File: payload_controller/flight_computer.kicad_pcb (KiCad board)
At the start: 4 copper layers, 87 x 75 mm, 145 parts, among them J1 Silicon Cell, J2 G125-MH12605M4R, J3 Conn_01x08_Female, J4 Conn_02x07_Odd_Even, J5 0781710004, J6 Conn_01x03_Male, Q1 DMC2053UVT, U1 74HC590, U10 OPA2387, U11 MCP4725xxx-xCH, U12 ADS131M04IPWR, U13 INA190A4IDDFR, U15 SN74LVC1G14DRL, U16 CD4518BM96, U17 CD4028BMT, U18 CD4028BMT, U19 MAX4736EUBT, U2 ADG841YKSZ-500RL7, U20 MAX4736EUBT, U21 MAX4736EUBT, U22 MAX4736EUBT, U23 MAX4736EUBT, U24 MAX4736EUBT, U25 MAX4736EUBT, U26 MAX4736EUBT, U27 MAX4736EUBT, U28 MAX4736EUBT, U29 MAX4736EUBT, U3 ADG841YKSZ-500RL7, U30 LT3092EDD#TRPBF, U31 LT6654AMPS6-1.25, U33 ICL7660CSAT, U34 MSP430FR5969IRGZR, U4 ADG841YKSZ-500RL7, U5 ADG841YKSZ-500RL7, U6 ADG841YKSZ-500RL7, U7 ADG841YKSZ-500RL7, U8 ADG841YKSZ-500RL7, U9 ADG841YKSZ-500RL7, Y1 CM8V-T1A

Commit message: Continuing layout
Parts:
- moved R28 17.0 mm to (178.9, 129.4), turned to 270 degrees
- moved R29 13.7 mm to (180.5, 129.4), turned to 270 degrees
- moved C11 8.41 mm to (156.0, 113.8), turned to 0 degrees
- moved R30 7.15 mm to (183.8, 132.0)
- moved Q1 7.08 mm to (183.9, 129.4), turned to 0 degrees
- moved R12 6.65 mm to (140.3, 115.1), turned to 270 degrees
- moved C10 5.72 mm to (146.6, 96.1)
- moved U1 5.71 mm to (152.7, 96.1)
- moved U10 4.72 mm to (156.0, 116.0), turned to 0 degrees
- moved J4 4.57 mm to (119.4, 97.0)
- moved C41 3.80 mm to (186.9, 131.2)
- moved C37 3.05 mm to (158.8, 69.3)
- moved C38 3.05 mm to (144.5, 74.2)
- moved C39 3.05 mm to (158.8, 77.2)
- moved C40 3.05 mm to (146.5, 85.2)
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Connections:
- net /Payload Controller/BUSY_IN renamed Net-(U34-Pad19)
- J2 pad 10: /Perovskite Switches/ALERT -> /Payload Controller/ALERT
- J2 pad 25: /Perovskite Switches/ALERT -> /Payload Controller/ALERT
- J2 pad 7: /Perovskite Switches/ALERT -> /Payload Controller/ALERT
- J3 pad 5: FAULT -> PAYLOAD_RST
- J3 pad 6: PAYLOAD_RST -> FAULT
- U10 pad 1: /Curve Tracer/LADDER_VOLTAGE -> Net-(R23-Pad2)
- U10 pad 2: /Curve Tracer/LADDER_VOLTAGE -> Net-(R23-Pad2)
- U10 pad 3: Net-(R11-Pad2) -> Net-(R25-Pad1)
- U10 pad 5: Net-(R25-Pad1) -> /Curve Tracer/LADDER_VOLTAGE
- U10 pad 6: Net-(R23-Pad2) -> Net-(R11-Pad2)
- U10 pad 7: Net-(R23-Pad2) -> /Curve Tracer/LADDER_VOLTAGE
- U19 pad 10: Net-(J2-Pad1) -> Net-(U19-Pad10)
- U19 pad 2: GND -> /Perovskite Switches/PANEL_POSITIVE
- U19 pad 4: /Perovskite Switches/PANEL_POSITIVE -> GND
- U19 pad 6: Net-(U19-Pad6) -> Net-(J2-Pad1)
- U19 pad 7: GND -> /Perovskite Switches/PANEL_POSITIVE
- U19 pad 9: /Perovskite Switches/PANEL_POSITIVE -> GND
- U20 pad 1: Net-(U17-Pad14) -> Net-(U17-Pad9)
- U20 pad 2: Net-(U19-Pad6) -> Net-(U19-Pad10)
- U20 pad 4: Net-(U19-Pad6) -> Net-(U19-Pad10)
- U20 pad 5: Net-(U17-Pad15) -> Net-(U17-Pad7)
- U21 pad 1: Net-(U17-Pad2) -> Net-(U17-Pad6)
- U21 pad 2: Net-(U19-Pad6) -> Net-(U19-Pad10)
- U21 pad 4: Net-(U19-Pad6) -> Net-(U19-Pad10)
- U21 pad 5: Net-(U17-Pad1) -> Net-(U17-Pad5)
- U22 pad 2: Net-(U19-Pad6) -> Net-(U19-Pad10)
- U22 pad 4: Net-(U19-Pad6) -> Net-(U19-Pad10)
- U23 pad 1: Net-(U17-Pad6) -> Net-(U17-Pad2)
- U23 pad 2: Net-(U19-Pad6) -> Net-(U19-Pad10)
- U23 pad 4: Net-(U19-Pad6) -> Net-(U19-Pad10)
- U23 pad 5: Net-(U17-Pad5) -> Net-(U17-Pad1)
- U24 pad 1: Net-(U17-Pad9) -> Net-(U17-Pad14)
- U24 pad 2: Net-(U19-Pad6) -> Net-(U19-Pad10)
- U24 pad 4: Net-(U19-Pad6) -> Net-(U19-Pad10)
- U24 pad 5: Net-(U17-Pad7) -> Net-(U17-Pad15)
- U25 pad 1: Net-(U18-Pad14) -> Net-(U18-Pad9)
- U25 pad 2: Net-(U19-Pad6) -> Net-(U19-Pad10)
- U25 pad 4: Net-(U19-Pad6) -> Net-(U19-Pad10)
- U25 pad 5: Net-(U18-Pad15) -> Net-(U18-Pad7)
- U26 pad 1: Net-(U18-Pad2) -> Net-(U18-Pad6)
- U26 pad 2: Net-(U19-Pad6) -> Net-(U19-Pad10)
- U26 pad 4: Net-(U19-Pad6) -> Net-(U19-Pad10)
- U26 pad 5: Net-(U18-Pad1) -> Net-(U18-Pad5)
- U27 pad 2: Net-(U19-Pad6) -> Net-(U19-Pad10)
- U27 pad 4: Net-(U19-Pad6) -> Net-(U19-Pad10)
- U28 pad 1: Net-(U18-Pad6) -> Net-(U18-Pad2)
- U28 pad 2: Net-(U19-Pad6) -> Net-(U19-Pad10)
- U28 pad 4: Net-(U19-Pad6) -> Net-(U19-Pad10)
- U28 pad 5: Net-(U18-Pad5) -> Net-(U18-Pad1)
- U29 pad 1: Net-(U18-Pad9) -> Net-(U18-Pad14)
- U29 pad 2: Net-(U19-Pad6) -> Net-(U19-Pad10)
- U29 pad 4: Net-(U19-Pad6) -> Net-(U19-Pad10)
- U29 pad 5: Net-(U18-Pad7) -> Net-(U18-Pad15)
- U34 pad 33: Net-(U34-Pad33) -> /Payload Controller/ALERT
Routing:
- net /Payload Controller/SCL: track 0.00 -> 184.1 mm, vias 0 -> 3
- net /Payload Controller/SDA: track 0.00 -> 179.4 mm, vias 0 -> 3
- net /Payload Controller/ALERT: track 0.00 -> 126.4 mm
- net Net-(U19-Pad10): track 0.00 -> 91.6 mm
- net +3V3: track 0.00 -> 80.5 mm, vias 0 -> 69
- net Net-(J2-Pad1): track 0.00 -> 63.1 mm
- net Net-(U18-Pad15): track 0.00 -> 57.5 mm
- net Net-(U18-Pad14): track 0.00 -> 55.9 mm
- net GND: track 0.00 -> 53.2 mm, vias 0 -> 43
- net Net-(U17-Pad15): track 0.00 -> 47.8 mm
- net Net-(U17-Pad14): track 0.00 -> 47.6 mm
- net Net-(U18-Pad1): track 0.00 -> 46.0 mm
- net Net-(U18-Pad2): track 0.00 -> 43.0 mm
- net Net-(U17-Pad1): track 0.00 -> 39.1 mm
- net Net-(U17-Pad2): track 0.00 -> 38.9 mm
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- added copper zone on In1.Cu, net -3V3

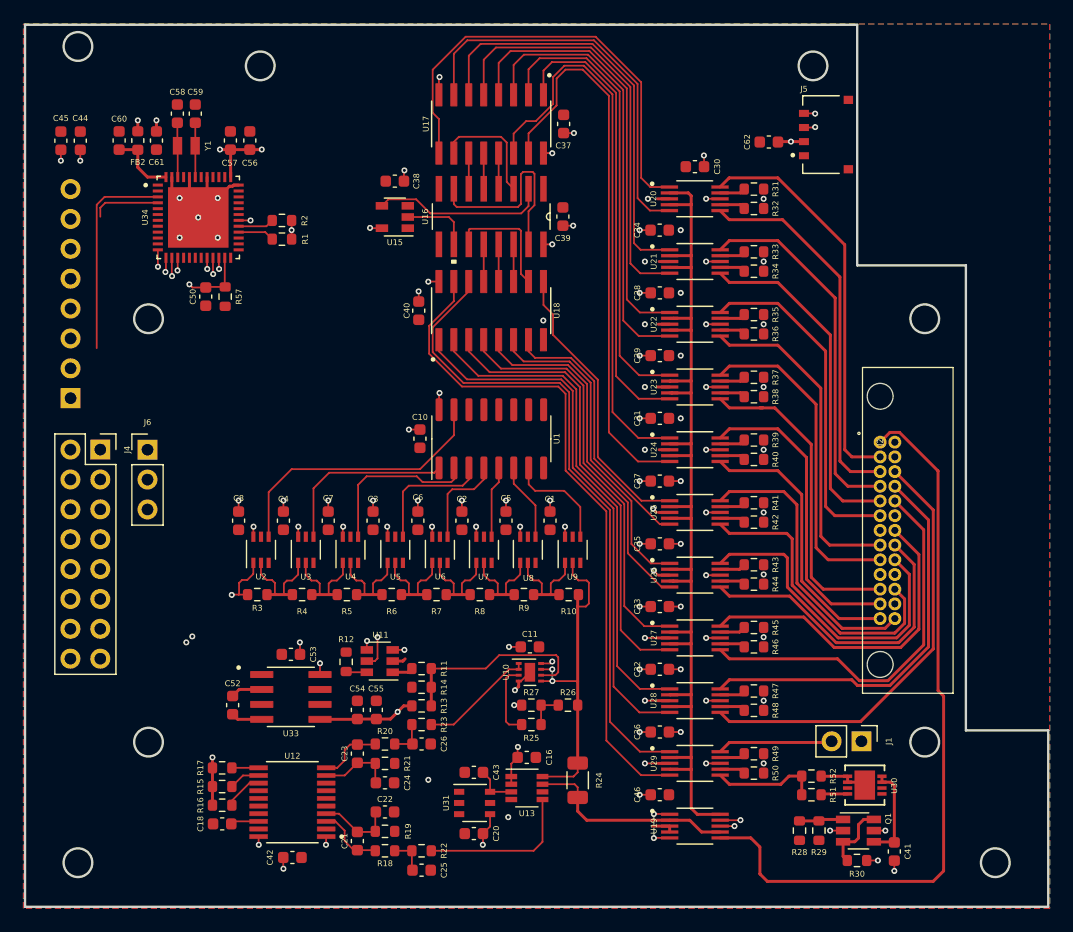
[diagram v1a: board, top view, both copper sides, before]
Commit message: Continuing payload design
- Add OR gate for reverse bias
- Add GaAs panel connectors
- Add 3D models
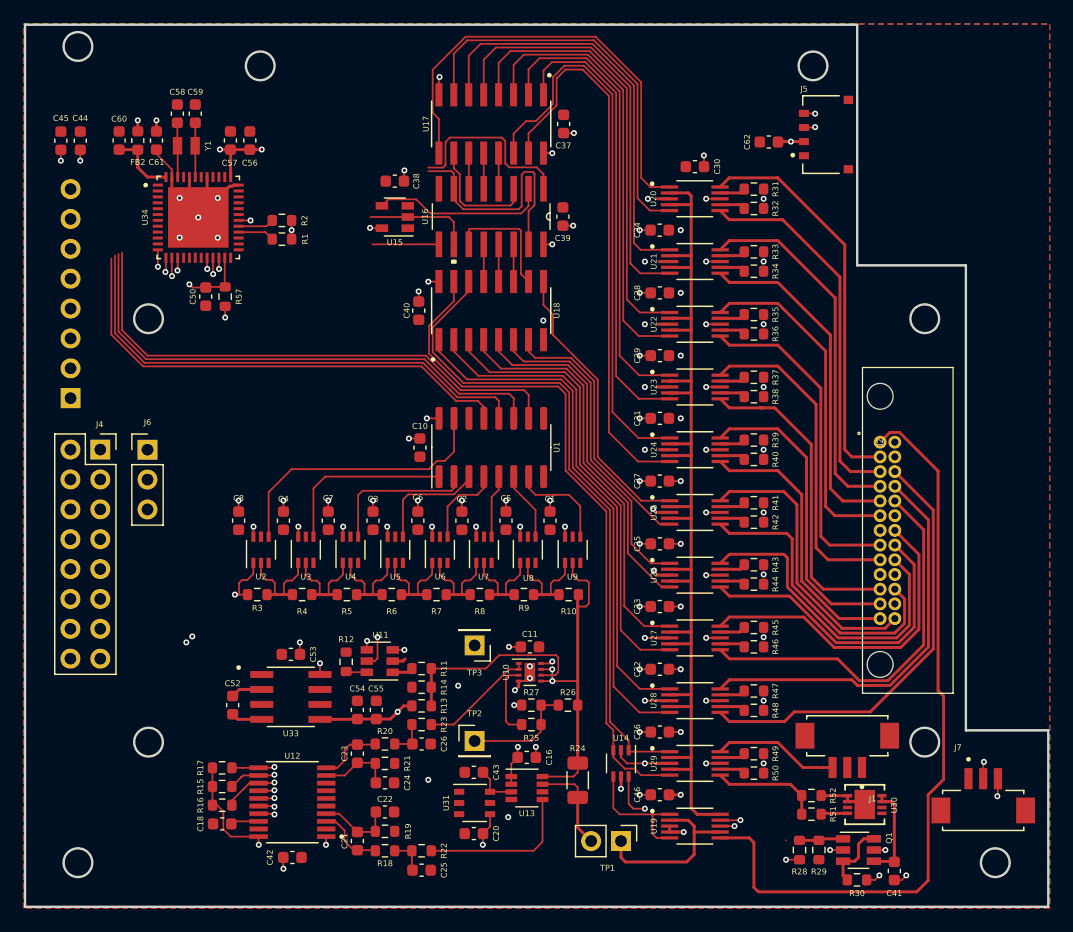
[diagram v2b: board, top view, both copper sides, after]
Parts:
- added J7: GaAs Temp, DF13C-3P-1:HRS_DF13C-3P-1.25V(21), F.Cu at (194.5, 127.7)
- added TP1: Current Test, Connector_PinHeader_2.54mm:PinHeader_1x02_P2.54mm_Vertical, F.Cu at (163.7, 130.3)
- added TP2: Voltage Test+, Connector_PinHeader_2.54mm:PinHeader_1x01_P2.54mm_Vertical, F.Cu at (151.3, 121.8)
- added TP3: Voltage Test-, Connector_PinHeader_2.54mm:PinHeader_1x01_P2.54mm_Vertical, F.Cu at (151.3, 113.7)
- added U14: 74LVC1G332, ul_ADG841YKSZ-500RL7:ADG841YKSZ-500RL7, F.Cu at (163.7, 123.7)
- J1: value Silicon Cell -> GaAs Cell; footprint Connector_PinHeader_2.54mm:PinHeader_1x02_P2.54mm_Vertical -> DF13C-3P-1:HRS_DF13C-3P-1.25V(21)
- moved C41 1.65 mm to (186.9, 132.8)
- moved R30 1.65 mm to (183.8, 133.6)
- moved R51 1.65 mm to (179.9, 128.0)
- moved R52 1.65 mm to (179.9, 126.4)
- moved U30 1.65 mm to (184.4, 127.2)
- moved Q1 1.65 mm to (183.9, 131.1)
- moved R28 1.65 mm to (178.9, 131.1)
- moved R29 1.65 mm to (180.5, 131.1)
- moved J1 1.29 mm to (182.9, 121.3), turned to 180 degrees
- moved C10 0.76 mm to (146.6, 96.9)
- moved U1 0.74 mm to (152.7, 96.8)
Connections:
- J1 pad 1: Net-(J1-Pad1) -> GND
- J4 pad 11: ~PAYLOAD_RST -> PAYLOAD_RST
- R24 pad 2: /Perovskite Switches/PANEL_POSITIVE -> Net-(R24-Pad2)
- U13 pad 7: /Perovskite Switches/PANEL_POSITIVE -> Net-(R24-Pad2)
- U19 pad 1: /Payload Controller/REVERSE_BIAS -> Net-(U14-Pad4)
- U19 pad 5: /Payload Controller/REVERSE_BIAS -> Net-(U14-Pad4)
- U29 pad 10: Net-(J1-Pad2) -> Net-(J1-Pad3)
- U34 pad 10: /Payload Controller/~LADDER_RESET -> /Payload Controller/LADDER_CLOCK
- U34 pad 11: /Payload Controller/LADDER_LATCH -> /Payload Controller/~LADDER_RESET
- U34 pad 24: /Payload Controller/ENABLE_PANEL_SWITCH -> /Payload Controller/10-19_CLOCK
- U34 pad 25: /Payload Controller/RESET_PANEL_SWITCH -> /Payload Controller/ENABLE_PANEL_SWITCH
- U34 pad 3: /Payload Controller/~LADDER_EN -> /Payload Controller/LADDER_LATCH
- U34 pad 34: /Payload Controller/10-19_CLOCK -> /Payload Controller/RESET_PANEL_SWITCH
- U34 pad 9: /Payload Controller/LADDER_CLOCK -> /Payload Controller/~LADDER_EN
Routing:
- net /Perovskite Switches/GAAS_TEMP: track 0.00 -> 122.5 mm, vias 0 -> 1
- net /Payload Controller/ENABLE_TEST_SOURCE: track 0.00 -> 95.5 mm, vias 0 -> 1
- net /Payload Controller/REVERSE_BIAS: track 4.75 -> 91.0 mm, vias 2 -> 1
- net /Curve Tracer/ADC_CLK: track 0.00 -> 45.8 mm, vias 0 -> 1
- net /Curve Tracer/MOSI: track 0.00 -> 44.9 mm, vias 0 -> 1
- net /Payload Controller/~LADDER_RESET: track 0.00 -> 44.7 mm
- net /Curve Tracer/MISO: track 0.00 -> 43.8 mm, vias 0 -> 1
- net /Payload Controller/LADDER_CLOCK: track 0.00 -> 43.5 mm
- net /Curve Tracer/SCLK: track 0.00 -> 42.6 mm, vias 0 -> 1
- net /Payload Controller/LADDER_LATCH: track 0.00 -> 41.7 mm
- net /Curve Tracer/ADC_CS: track 2.66 -> 43.2 mm, vias 0 -> 1
- net /Curve Tracer/ADC_SYNC: track 2.28 -> 41.6 mm, vias 0 -> 1
- net /Curve Tracer/ADC_DRDY: track 9.11 -> 44.7 mm, vias 0 -> 1
- net PAYLOAD_RST: track 16.1 -> 46.5 mm
- net /Payload Controller/~LADDER_EN: track 17.7 -> 43.1 mm
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
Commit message: Completed routing
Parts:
- added TP4: ADC_CLK Connect, TestPoint:TestPoint_2Pads_Pitch2.54mm_Drill0.8mm, F.Cu at (122.7, 133.3)
- added X1: CB3LV-3I-8M1920, CB3LV-3I-8M1920:OSCCC700X500X180-4N, F.Cu at (123.9, 128.2)
- TP1: footprint Connector_PinHeader_2.54mm:PinHeader_1x02_P2.54mm_Vertical -> TestPoint:TestPoint_2Pads_Pitch2.54mm_Drill0.8mm
- moved R1 2.29 mm to (137.2, 79.1)
- moved R2 2.29 mm to (137.2, 77.5)
- turned TP1 to 180 degrees
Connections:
- J7 pad 3: /Perovskite Switches/GAAS_TEMP -> /Payload Controller/GAAS_TEMP
- U12 pad 17: /Curve Tracer/ADC_CLK -> Net-(TP4-Pad2)
- U34 pad 1: Net-(U34-Pad1) -> /Payload Controller/REVERSE_BIAS
- U34 pad 16: /Payload Controller/ENABLE_TEST_SOURCE -> /Payload Controller/ALERT
- U34 pad 17: /Curve Tracer/ADC_CS -> /Payload Controller/GAAS_TEMP
- U34 pad 18: /Curve Tracer/ADC_CLK -> /Payload Controller/ENABLE_TEST_SOURCE
- U34 pad 19: Net-(U34-Pad19) -> /Curve Tracer/ADC_CLK
- U34 pad 2: Net-(U34-Pad2) -> /Payload Controller/LADDER_LATCH
- U34 pad 27: Net-(U34-Pad27) -> FAULT
- U34 pad 3: /Payload Controller/LADDER_LATCH -> /Payload Controller/~LADDER_EN
- U34 pad 30: FAULT -> Net-(U34-Pad30)
- U34 pad 33: /Payload Controller/ALERT -> Net-(U34-Pad33)
- U34 pad 39: /Payload Controller/REVERSE_BIAS -> Net-(U34-Pad39)
- U34 pad 9: /Payload Controller/~LADDER_EN -> /Curve Tracer/ADC_CS
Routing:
- net /Payload Controller/GAAS_TEMP: track 0.00 -> 131.8 mm, vias 0 -> 2
- net /Perovskite Switches/GAAS_TEMP: track 122.5 -> 0.00 mm, vias 1 -> 0
- net /Curve Tracer/ADC_SYNC: track 41.6 -> 75.7 mm, vias 1 -> 2
- net /Curve Tracer/ADC_DRDY: track 44.7 -> 70.7 mm, vias 1 -> 4
- net /Payload Controller/REVERSE_BIAS: track 91.0 -> 116.0 mm, vias 1 -> 2
- net /Curve Tracer/ADC_CS: track 43.2 -> 65.8 mm, vias 1 -> 4
- net /Curve Tracer/MISO: track 43.8 -> 62.2 mm, vias 1 -> 2
- net /Payload Controller/SDA: track 203.4 -> 221.2 mm, vias 3 -> 4
- net /Payload Controller/SCL: track 207.6 -> 225.1 mm, vias 3 -> 4
- net /Payload Controller/RESET_PANEL_SWITCH: track 20.9 -> 38.3 mm
- net /Payload Controller/0-9_CLOCK: track 15.6 -> 33.0 mm
- net /Curve Tracer/MOSI: track 44.9 -> 62.1 mm, vias 1 -> 2
- net Net-(TP4-Pad2): track 0.00 -> 16.3 mm
- net /Curve Tracer/SCLK: track 42.6 -> 58.6 mm, vias 1 -> 2
- net /Curve Tracer/ADC_CLK: track 45.8 -> 61.5 mm, vias 1 -> 2
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
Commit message: Generated manufacturing files
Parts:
- removed TP1: Current Test, TestPoint:TestPoint_2Pads_Pitch2.54mm_Drill0.8mm
- removed TP2: Voltage Test+, Connector_PinHeader_2.54mm:PinHeader_1x01_P2.54mm_Vertical
- removed TP3: Voltage Test-, Connector_PinHeader_2.54mm:PinHeader_1x01_P2.54mm_Vertical
- removed TP4: ADC_CLK Connect, TestPoint:TestPoint_2Pads_Pitch2.54mm_Drill0.8mm
- added CLK: ADC_CLK Connect, TestPoint:TestPoint_2Pads_Pitch2.54mm_Drill0.8mm, F.Cu at (122.7, 133.3)
- added CURRENT: Current Test, TestPoint:TestPoint_2Pads_Pitch2.54mm_Drill0.8mm, F.Cu at (163.7, 130.3)
- added G***: LOGO, AXP Logos:bigred_logo, B.Cu at (150.9, 113.1)
- added G***: LOGO, AXP Logos:axp_logos, B.Cu at (151.3, 80.0)
- added V+: Voltage Test+, Connector_PinHeader_2.54mm:PinHeader_1x01_P2.54mm_Vertical, F.Cu at (151.3, 121.8)
- added V-: Voltage Test-, Connector_PinHeader_2.54mm:PinHeader_1x01_P2.54mm_Vertical, F.Cu at (151.3, 113.7)
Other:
- board text added: "Big Red Payload Controller Rev A Aerospace eXperimental Payloads UNL Aerospace Club Copyright c 2022"
